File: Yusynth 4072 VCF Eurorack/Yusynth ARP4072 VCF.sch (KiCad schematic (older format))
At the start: 78 parts, among them J1 Audio In 1, J2 Audio In 2, J3 V/Oct, J4 CV 1, J5 CV 2, J6 Audio In 1, J7 CONN_02X05, Q1 MMDT3906, Q2 MMDT3906, Q3 MMDT3906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

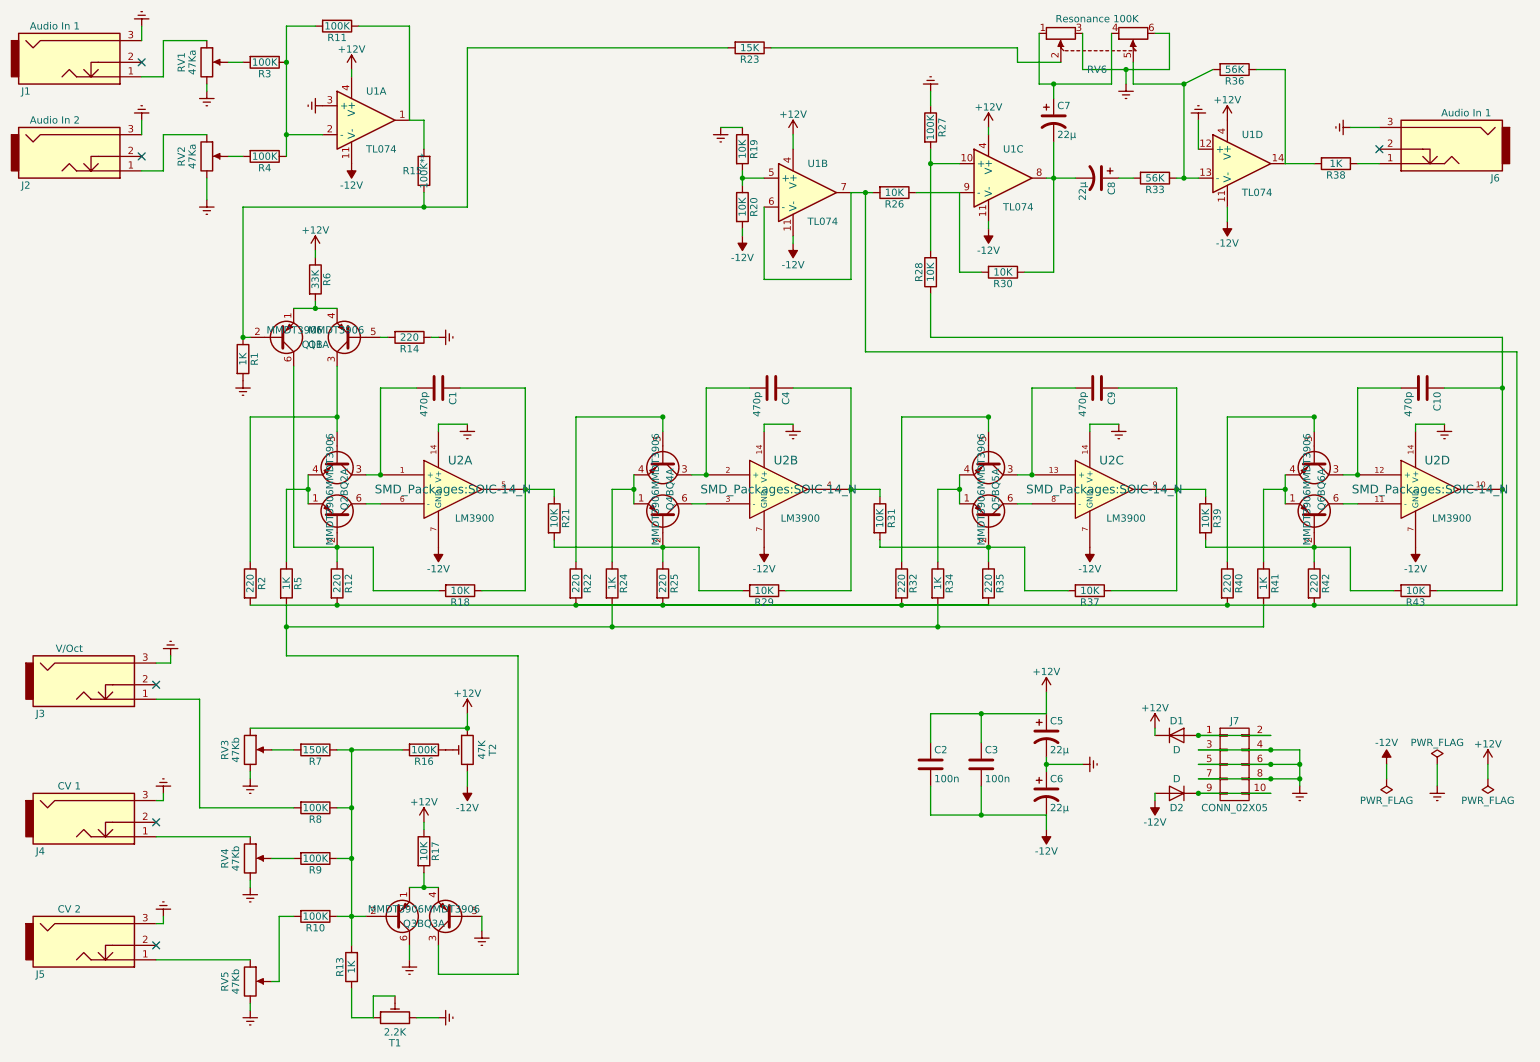
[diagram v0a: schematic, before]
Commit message: Fixed LM3900 pin mapping. File cleanup
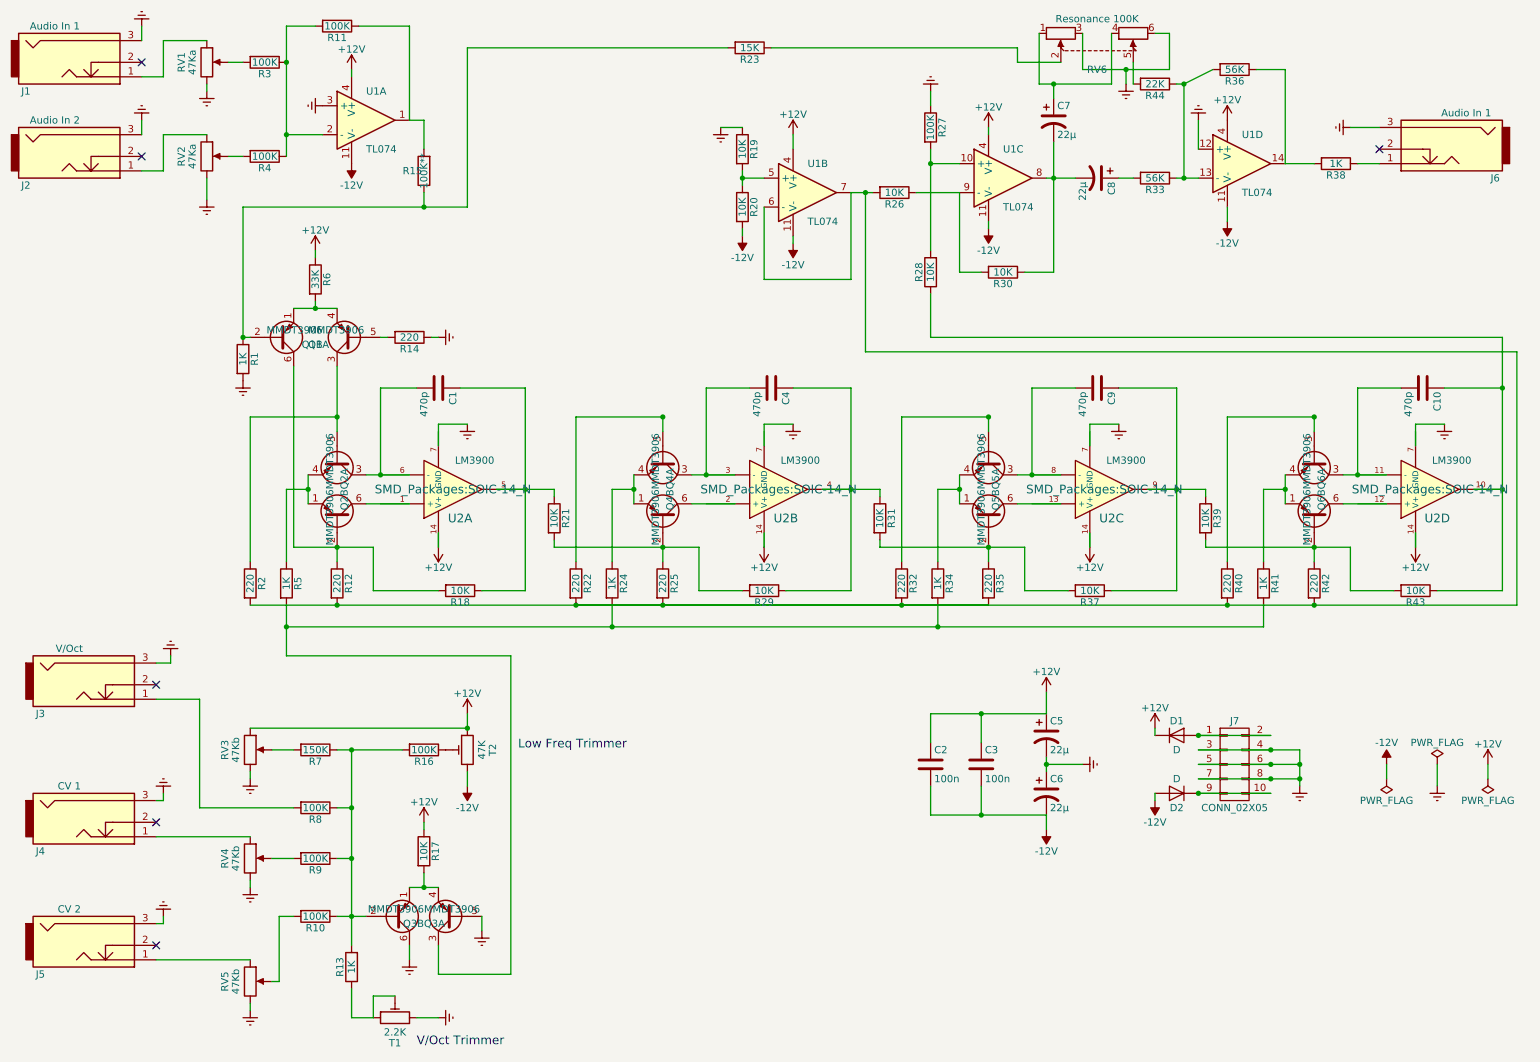
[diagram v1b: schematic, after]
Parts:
- added R44: 22K, Resistors_SMD:R_0603, symbol R
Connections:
- wire segments 247 -> 248
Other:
- note added: "Low Freq Trimmer"
- note added: "V/Oct Trimmer\n"

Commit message: fixed power routing to LM3900
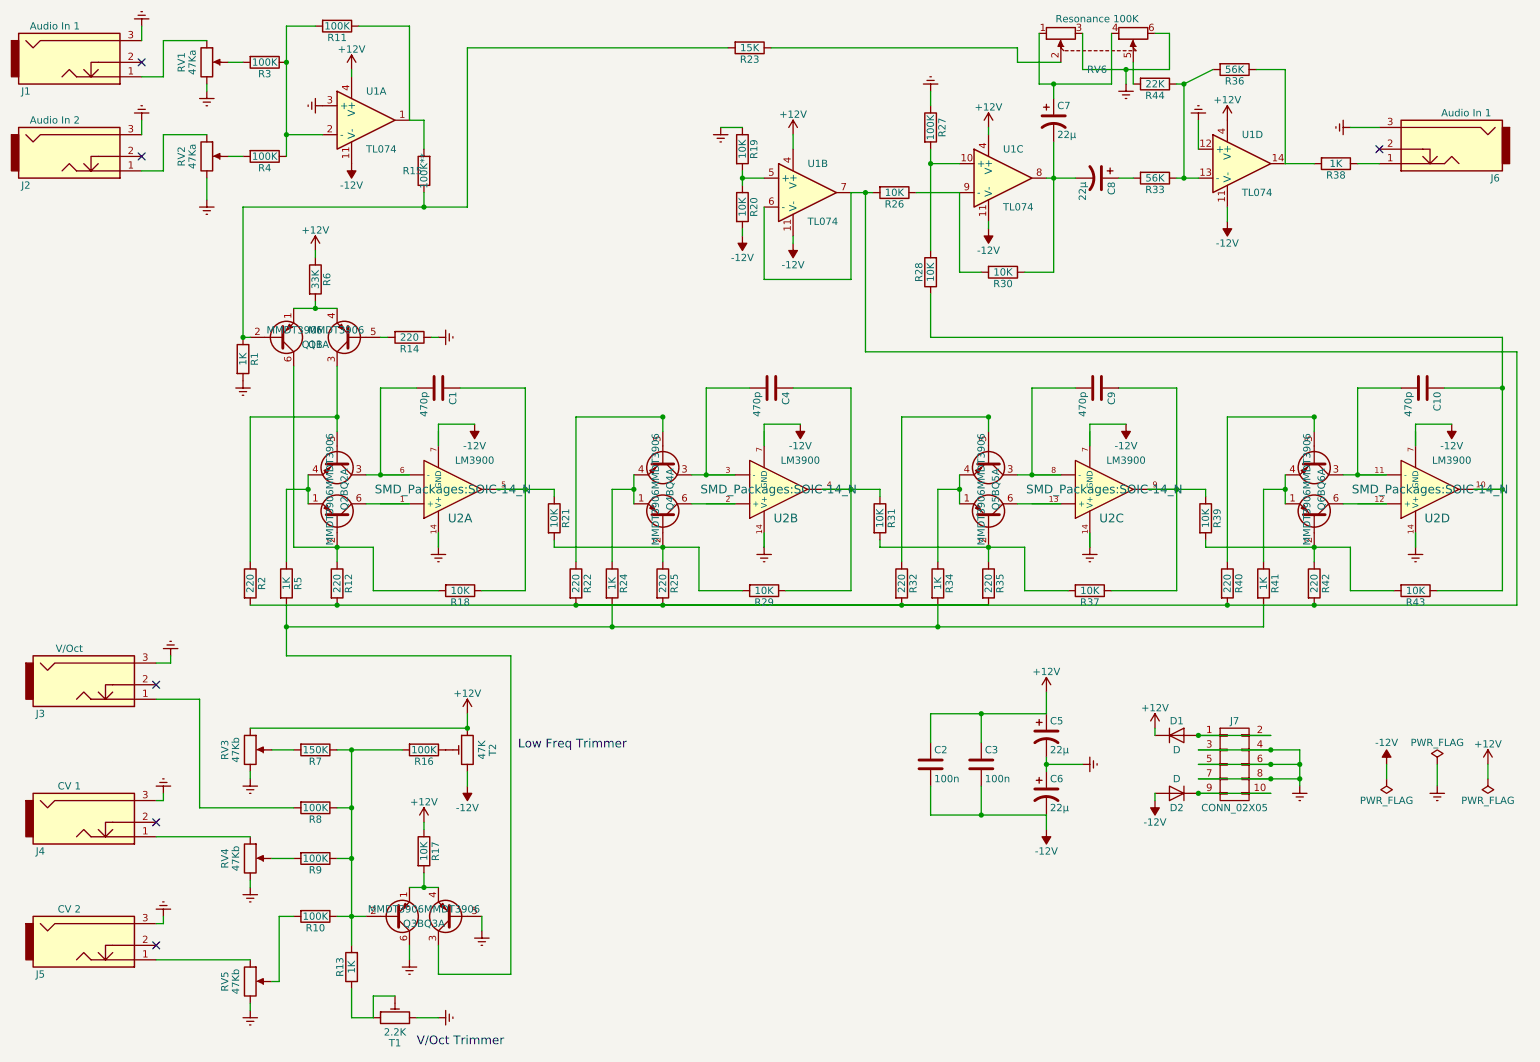
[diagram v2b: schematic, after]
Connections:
- wire segments 248 -> 306

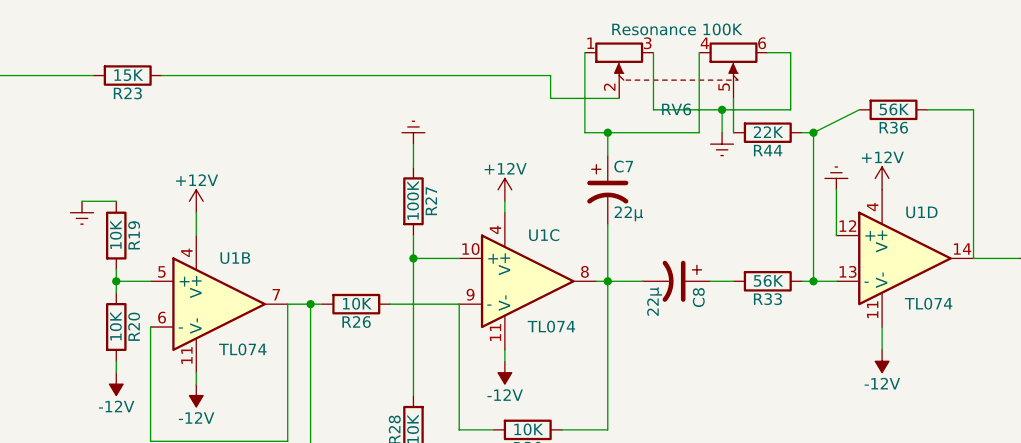
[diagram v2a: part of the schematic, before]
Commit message: Changed dual-gang pot to single gang for easier sourcing. Rotated pot footprints
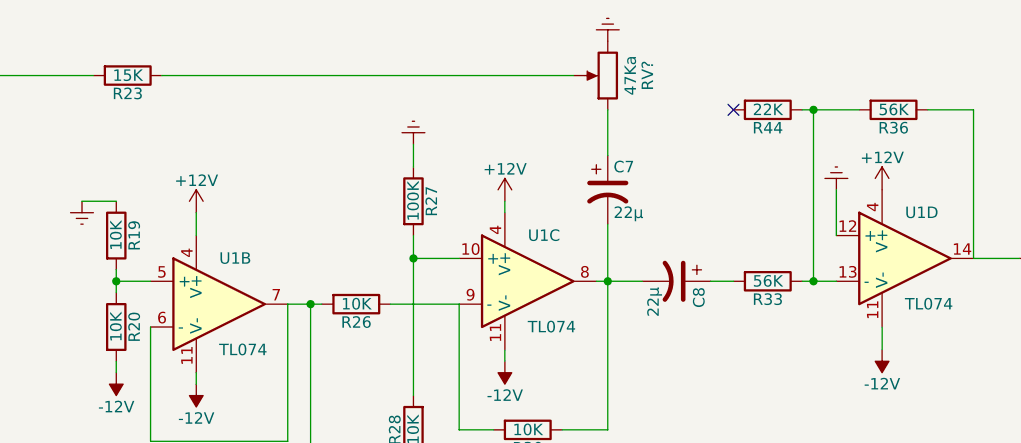
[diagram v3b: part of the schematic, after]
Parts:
- removed RV6: Resonance 100K, Potentiometers:Potentiometer_Alps_RK09L_Double_Horizontal, symbol POT_Dual
- added RV?: 47Ka, Potentiometers:Potentiometer_Alps_RK09L_Sleve_Single_Horizontal, symbol POT
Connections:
- wire segments 306 -> 293
- no-connect marks 6 -> 7
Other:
- moved on the sheet: R44
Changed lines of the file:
@@
 LIBS:contrib
 LIBS:valves
+LIBS:Yusynth ARP4072 VCF-cache
 EELAYER 25 0
 EELAYER END
@@
 $EndComp
 $Comp
-L POT_Dual RV6
-U 1 1 59C64A2C
-P 8100 800
-F 0 "RV6" H 8100 950 50  0000 C CNN
-F 1 "Resonance 100K" H 8100 600 50  0000 C CNN
-F 2 "Potentiometers:Potentiometer_Alps_RK09L_Double_Horizontal" H 8350 725 50  0001 C CNN
-F 3 "" H 8350 725 50  0001 C CNN
-	1    8100 800
-	1    0    0    1
-$EndComp
-$Comp
-L Earth #PWR39
-U 1 1 59C659D1
-P 8300 1050
-F 0 "#PWR39" H 8300 800 50  0001 C CNN
-F 1 "Earth" H 8300 900 50  0001 C CNN
-F 2 "" H 8300 1050 50  0001 C CNN
-F 3 "" H 8300 1050 50  0001 C CNN
-	1    8300 1050
-	1    0    0    -1
-$EndComp
-$Comp
 L R R33
 U 1 1 59C66337
@@
 	3750 800  5550 800
 Wire Wire Line
-	5850 800  7550 800
-Wire Wire Line
-	7550 800  7550 900
-Wire Wire Line
-	7550 900  7850 900
-Wire Wire Line
-	8000 700  8000 950
-Wire Wire Line
-	8000 950  8300 950
-Wire Wire Line
-	8300 950  8600 950
-Wire Wire Line
-	8600 950  8600 700
-Wire Wire Line
-	8600 700  8500 700
-Connection ~ 8300 950
-Wire Wire Line
-	8300 950  8300 1050
-Wire Wire Line
-	7800 1150 7800 1050
-Wire Wire Line
-	7700 1050 7800 1050
-Wire Wire Line
-	7800 1050 8200 1050
-Wire Wire Line
-	7700 1050 7700 700
-Connection ~ 7800 1050
-Wire Wire Line
-	8200 1050 8200 700
+	5850 800  7650 800
+Wire Wire Line
+	7800 950  7800 1150
 Wire Wire Line
 	8350 1700 8250 1700
@@
 Connection ~ 8700 1700
 Wire Wire Line
-	8700 1700 8700 1050
-Wire Wire Line
-	8700 1050 8900 950
+	8700 1700 8700 950
+Wire Wire Line
+	8700 950  8900 950
 Wire Wire Line
 	9200 950  9400 950
 Wire Wire Line
 	9400 950  9400 1600
-Connection ~ 8700 1050
-Wire Wire Line
-	8350 1050 8350 900
+Connection ~ 8700 950
 Wire Wire Line
 	9400 1600 9600 1600
@@
 L R R44
 U 1 1 59F94363
-P 8500 1050
-F 0 "R44" V 8580 1050 50  0000 C CNN
-F 1 "22K" V 8500 1050 50  0000 C CNN
-F 2 "Resistors_SMD:R_0603" V 8430 1050 50  0001 C CNN
-F 3 "" H 8500 1050 50  0001 C CNN
-	1    8500 1050
-	0    1    1    0
-$EndComp
-Wire Wire Line
-	8700 1050 8650 1050
+P 8500 950
+F 0 "R44" V 8580 950 50  0000 C CNN
+F 1 "22K" V 8500 950 50  0000 C CNN
+F 2 "Resistors_SMD:R_0603" V 8430 950 50  0001 C CNN
+F 3 "" H 8500 950 50  0001 C CNN
+	1    8500 950
+	0    1    1    0
+$EndComp
+Wire Wire Line
+	8700 950  8650 950
 Text Notes 3400 7700 0    60   ~ 0
 V/Oct Trimmer\n
@@
 	1    0    0    -1
 $EndComp
+$Comp
+L POT RV?
+U 1 1 5A16FF74
+P 7800 800
+F 0 "RV?" V 7625 800 50  0000 C CNN
+F 1 "47Ka" V 7700 800 50  0000 C CNN
+F 2 "Potentiometers:Potentiometer_Alps_RK09L_Sleve_Single_Horizontal" H 7800 800 50  0001 C CNN
+F 3 "" H 7800 800 50  0001 C CNN
+	1    7800 800
+	-1   0    0    1
+$EndComp
+NoConn ~ 8350 950
+$Comp
+L Earth #PWR?
+U 1 1 5A171611
+P 7800 650
+F 0 "#PWR?" H 7800 400 50  0001 C CNN
+F 1 "Earth" H 7800 500 50  0001 C CNN
+F 2 "" H 7800 650 50  0001 C CNN
+F 3 "" H 7800 650 50  0001 C CNN
+	1    7800 650
+	-1   0    0    1
+$EndComp
 $EndSCHEMATC

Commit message: Trace updates
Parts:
- gave numbers to parts that had none: 1
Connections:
- wire segments 293 -> 236

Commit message: Minor corrections
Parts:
- J6: value Audio In 1 -> Audio Out
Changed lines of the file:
@@
 P 10500 1500
 F 0 "J6" H 10150 1300 50  0000 C CNN
-F 1 "Audio In 1" H 10350 1750 50  0000 C CNN
+F 1 "Audio Out" H 10350 1750 50  0000 C CNN
 F 2 "Thonkiconn:THONKICONN" H 10500 1500 50  0001 C CNN
 F 3 "" H 10500 1500 50  0001 C CNN

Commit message: updated board to use corrected thonkiconn lib. Wiring incomplete.
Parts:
- Q4, Q5: PN (none) -> MMDT3906-7-F
- R3: PN (none) -> RC0603FR-13100KL; Package (none) -> 0603
- RV6: value 47Ka -> 47Kb
- U2: PN (none) -> LM3900DR
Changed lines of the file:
@@
 F 2 "Resistors_SMD:R_0603" V 2280 900 50  0001 C CNN
 F 3 "" H 2350 900 50  0001 C CNN
+F 4 "0603" V 2350 900 60  0001 C CNN "Package"
+F 5 "RC0603FR-13100KL" V 2350 900 60  0001 C CNN "PN"
 	1    2350 900
 	0    1    1    0
@@
 F 2 "SMD_Packages:SOIC-14_N" H 5900 3850 60  0000 C CNN
 F 3 "" H 5900 3850 60  0000 C CNN
+F 4 "LM3900DR" H 5900 3850 60  0001 C CNN "PN"
 	2    5900 3850
 	1    0    0    1
@@
 F 2 "TO_SOT_Packages_SMD:SOT-363_SC-70-6" H 5300 4150 50  0001 C CNN
 F 3 "" H 5100 4050 50  0001 C CNN
+F 4 "MMDT3906-7-F" V 5100 4050 60  0001 C CNN "PN"
 	1    5100 4050
 	0    1    -1   0
@@
 F 2 "TO_SOT_Packages_SMD:SOT-363_SC-70-6" H 5300 3750 50  0001 C CNN
 F 3 "" H 5100 3650 50  0001 C CNN
+F 4 "MMDT3906-7-F" V 5100 3650 60  0001 C CNN "PN"
 	2    5100 3650
 	0    1    1    0
@@
 F 2 "TO_SOT_Packages_SMD:SOT-363_SC-70-6" H 7550 3750 50  0001 C CNN
 F 3 "" H 7350 3650 50  0001 C CNN
+F 4 "MMDT3906-7-F" V 7350 3650 60  0001 C CNN "PN"
 	2    7350 3650
 	0    1    1    0
@@
 P 7800 800
 F 0 "RV6" V 7625 800 50  0000 C CNN
-F 1 "47Ka" V 7700 800 50  0000 C CNN
+F 1 "47Kb" V 7700 800 50  0000 C CNN
 F 2 "Potentiometers:Potentiometer_Alps_RK09L_Sleve_Single_Horizontal" H 7800 800 50  0001 C CNN
 F 3 "" H 7800 800 50  0001 C CNN
